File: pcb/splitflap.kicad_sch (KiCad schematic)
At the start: 62 parts, among them J1 Motor D, J10 Hall C, J11 Hall B, J12 I2C, J2 Motor C, J3 Motor B, J4 Motor A, J5 Barrel_Jack_Switch, J6 USB_C_Receptacle_USB2.0_16P, J7 Barrel_Jack_Switch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

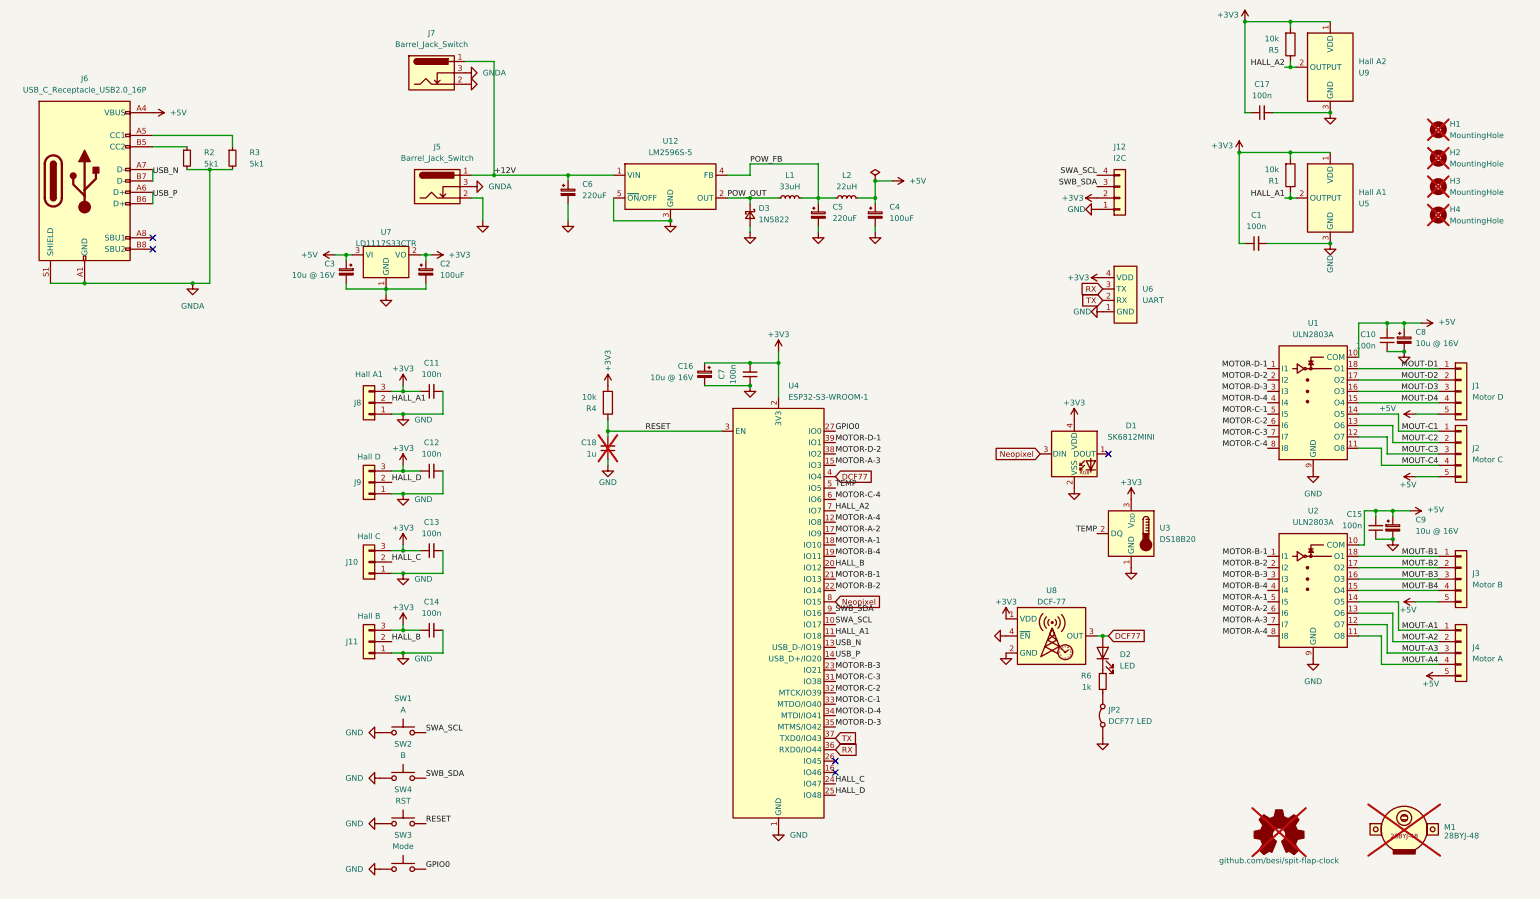
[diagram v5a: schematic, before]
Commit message: DNP components and bigger pads for hand solder items
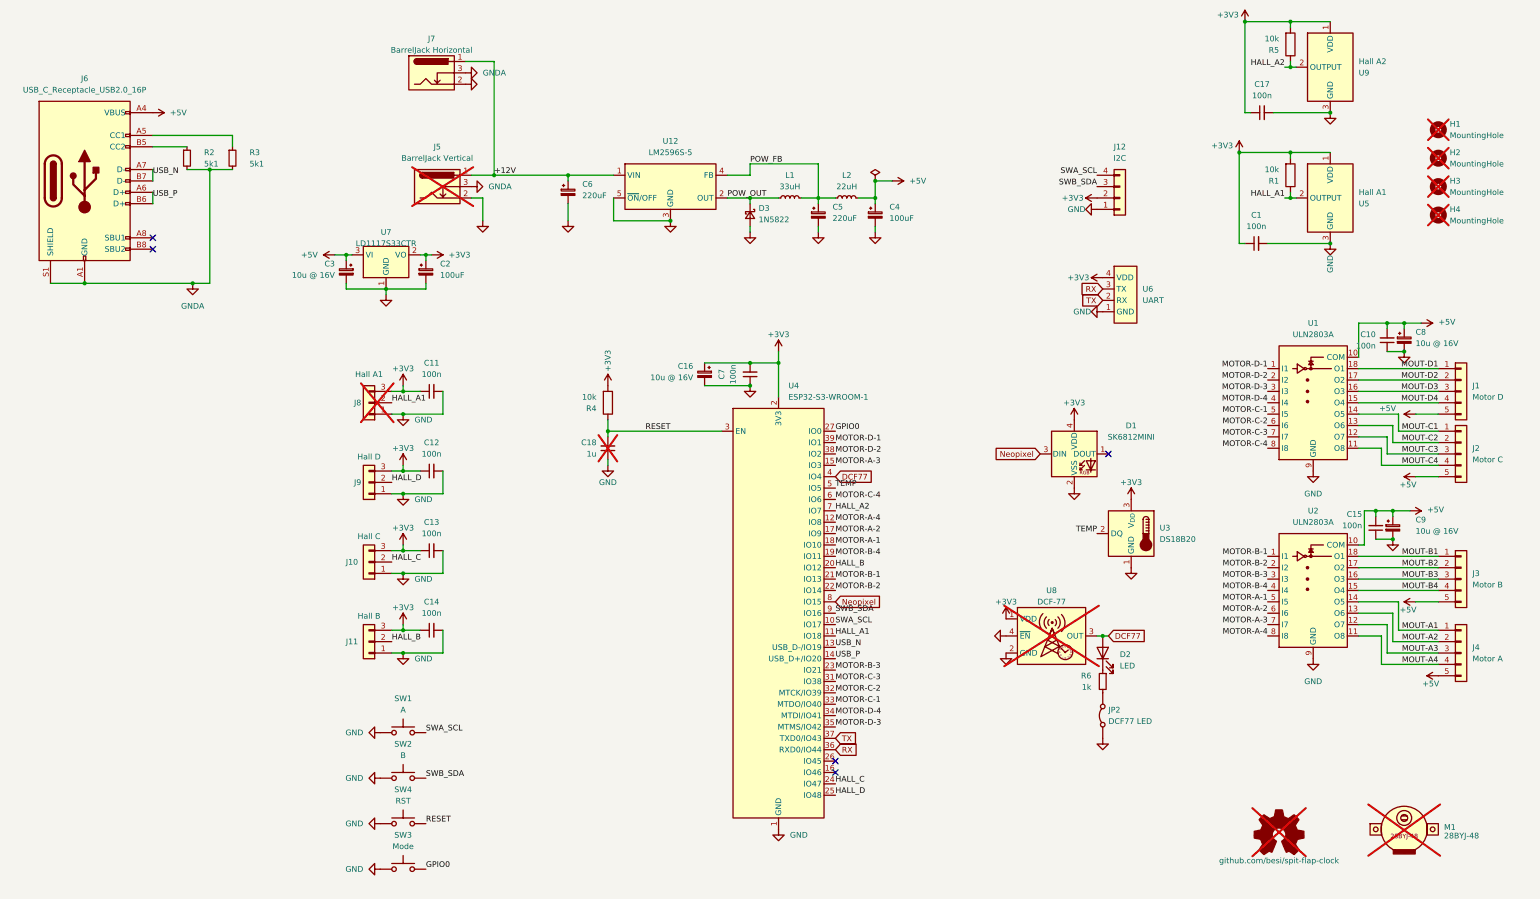
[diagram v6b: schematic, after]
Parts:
- J5: value Barrel_Jack_Switch -> BarrelJack Vertical; now not fitted; now left out of the parts list
- J7: value Barrel_Jack_Switch -> BarrelJack Horizontal
- J8, U8: now not fitted
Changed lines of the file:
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@@
 		(fields_autoplaced yes)
 		(property "Reference" "J7"
-			(at 43.18 -5.08 0)
+			(at 43.18 -3.81 0)
 			(effects
 				(font
@@
 			)
 		)
-		(property "Value" "Barrel_Jack_Switch"
-			(at 43.18 -2.54 0)
+		(property "Value" "BarrelJack Horizontal"
+			(at 43.18 -1.27 0)
 			(effects
 				(font
@@
 		(in_bom yes)
 		(on_board yes)
-		(dnp no)
+		(dnp yes)
 		(property "Reference" "J8"
 			(at 26.67 77.47 0)
@@
 		(unit 1)
 		(exclude_from_sim no)
-		(in_bom yes)
+		(in_bom no)
 		(on_board yes)
-		(dnp no)
+		(dnp yes)
 		(fields_autoplaced yes)
 		(property "Reference" "J5"
@@
 			)
 		)
-		(property "Value" "Barrel_Jack_Switch"
+		(property "Value" "BarrelJack Vertical"
 			(at 44.45 22.86 0)
 			(effects
@@
 		(in_bom yes)
 		(on_board yes)
-		(dnp no)
+		(dnp yes)
 		(fields_autoplaced yes)
 		(property "Reference" "U8"

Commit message: Run DRC
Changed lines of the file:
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@@
+	)
+	(symbol
+		(lib_id "power:PWR_FLAG")
+		(at 73.66 26.67 0)
+		(unit 1)
+		(exclude_from_sim no)
+		(in_bom yes)
+		(on_board yes)
+		(dnp no)
+		(fields_autoplaced yes)
+		(property "Reference" "#FLG01"
+			(at 73.66 24.765 0)
+			(effects
+				(font
+					(size 1.27 1.27)
+				)
+				(hide yes)
+			)
+		)
+		(property "Value" "PWR_FLAG"
+			(at 73.66 21.59 0)
+			(effects
+				(font
+					(size 1.27 1.27)
+				)
+			)
+		)
+		(property "Footprint" ""
+			(at 73.66 26.67 0)
+			(effects
+				(font
+					(size 1.27 1.27)
+				)
+				(hide yes)
+			)
+		)
+		(property "Datasheet" "~"
+			(at 73.66 26.67 0)
+			(effects
+				(font
+					(size 1.27 1.27)
+				)
+				(hide yes)
+			)
+		)
+		(property "Description" "Special symbol for telling ERC where power comes from"
+			(at 73.66 26.67 0)
+			(effects
+				(font
+					(size 1.27 1.27)
+				)
+				(hide yes)
+			)
+		)
+		(pin "1"
+		)
+		(instances
+			(project ""
+				(path "/f3b5a3df-7272-4af1-9be6-6c38555ab067"
+					(reference "#FLG01")
+					(unit 1)
+				)
+			)
+		)
 	)
 	(symbol

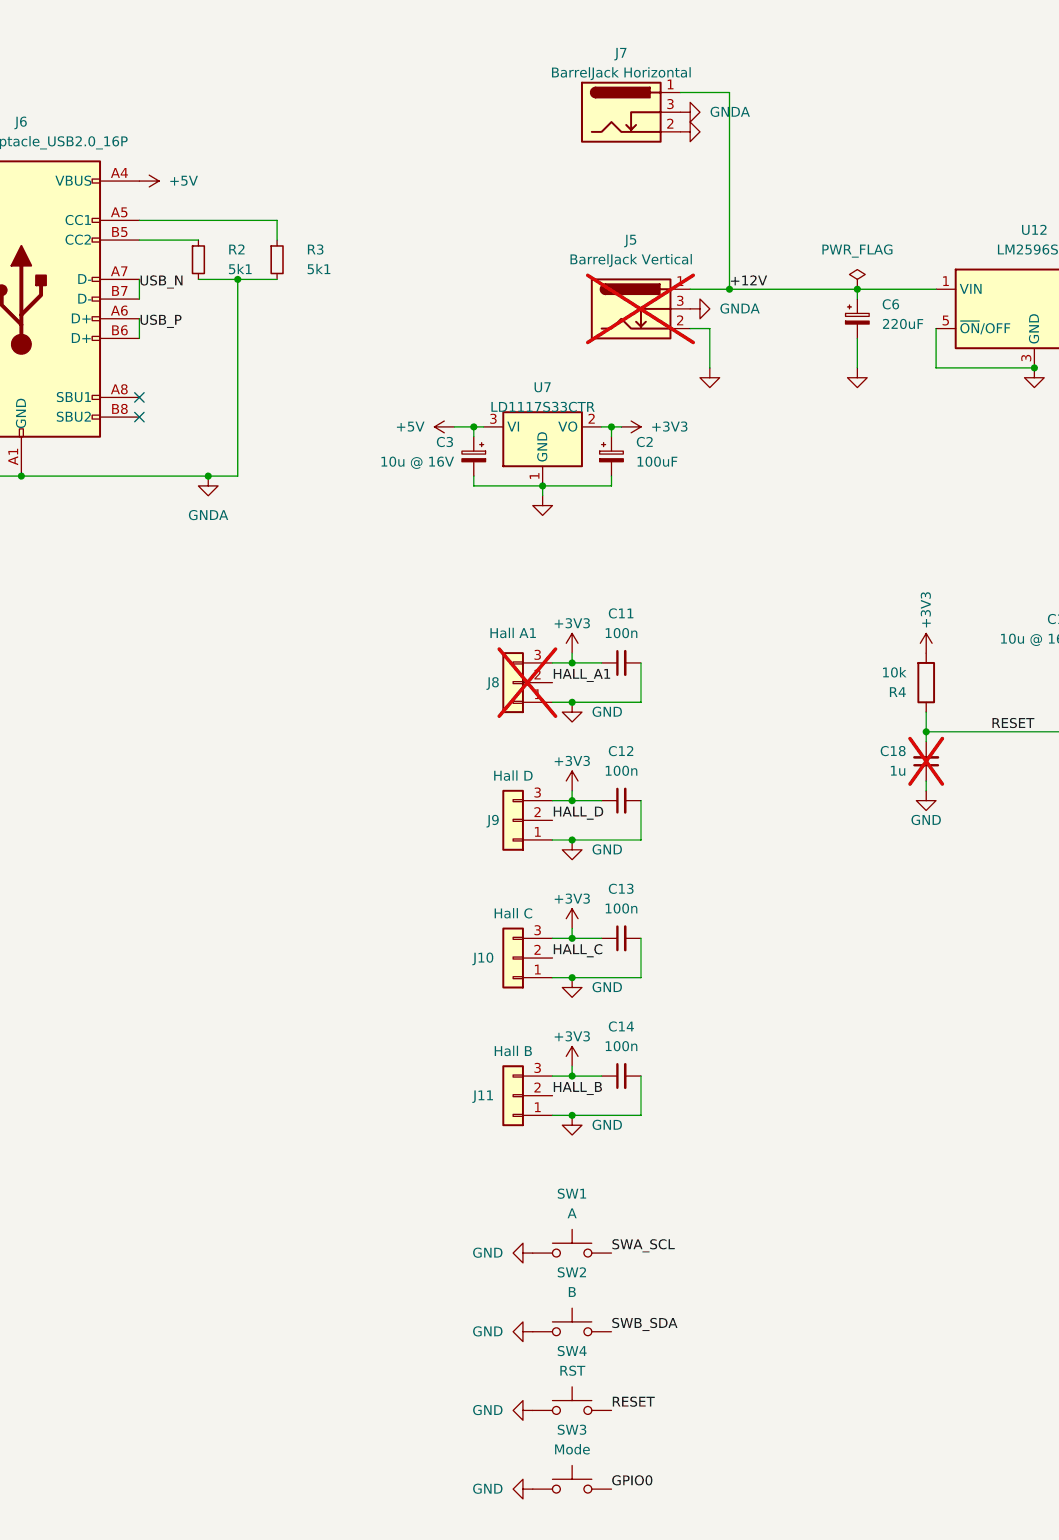
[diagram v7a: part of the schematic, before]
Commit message: Add test points for motor input signals and hall sensors
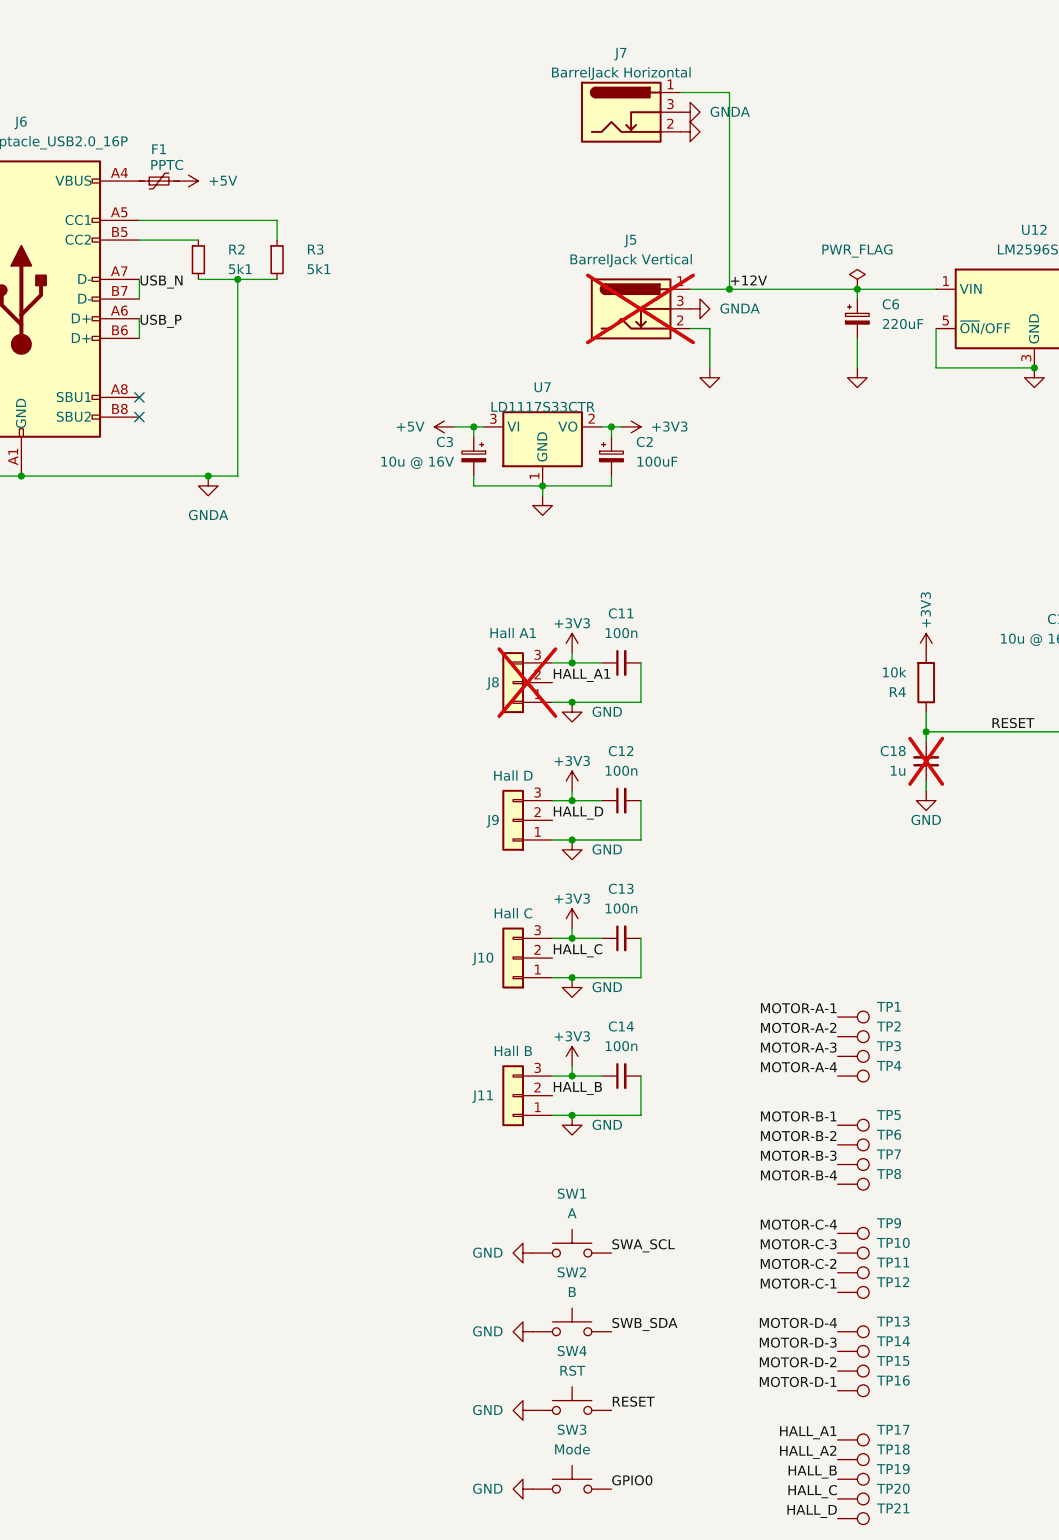
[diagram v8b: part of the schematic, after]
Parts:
- added F1: PPTC, Fuse:Fuse_1206_3216Metric, symbol Device:Polyfuse_Small
- added TP1, TP10, TP11, TP12, TP13, TP14, TP15, TP16, TP17, TP18, TP19, TP2, TP20, TP21, TP3, TP4, TP5, TP6, TP7, TP8, TP9: TestPoint, TestPoint:TestPoint_Pad_D1.0mm, symbol Connector:TestPoint
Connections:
- net +5V: now also F1.2; no longer J6.A4 (VBUS), J6.A9 (VBUS), J6.B4 (VBUS), J6.B9 (VBUS)
- net HALL_A1: now also TP17.1
- net HALL_A2: now also TP18.1
- net HALL_B: now also TP19.1
- net HALL_C: now also TP20.1
- net HALL_D: now also TP21.1
- net MOTOR-A-1: now also TP1.1
- net MOTOR-A-2: now also TP2.1
- net MOTOR-A-3: now also TP3.1
- net MOTOR-A-4: now also TP4.1
- net MOTOR-B-1: now also TP5.1
- net MOTOR-B-2: now also TP6.1
- net MOTOR-B-3: now also TP7.1
- net MOTOR-B-4: now also TP8.1
- net MOTOR-C-1: now also TP12.1
- net MOTOR-C-2: now also TP11.1
- net MOTOR-C-3: now also TP10.1
- net MOTOR-C-4: now also TP9.1
- net MOTOR-D-1: now also TP16.1
- net MOTOR-D-2: now also TP15.1
- net MOTOR-D-3: now also TP14.1
- net MOTOR-D-4: now also TP13.1
- new net: F1.1, J6.A4 (VBUS), J6.A9 (VBUS), J6.B4 (VBUS), J6.B9 (VBUS)
